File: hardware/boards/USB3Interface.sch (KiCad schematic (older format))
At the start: 7 parts, among them J2 USB3_Micro_B_Amphenol, J5 Conn_02x04_Odd_Even, U1 ECP5UM5G-381caBGA, U3 CYUSB3014, U6 128MiB

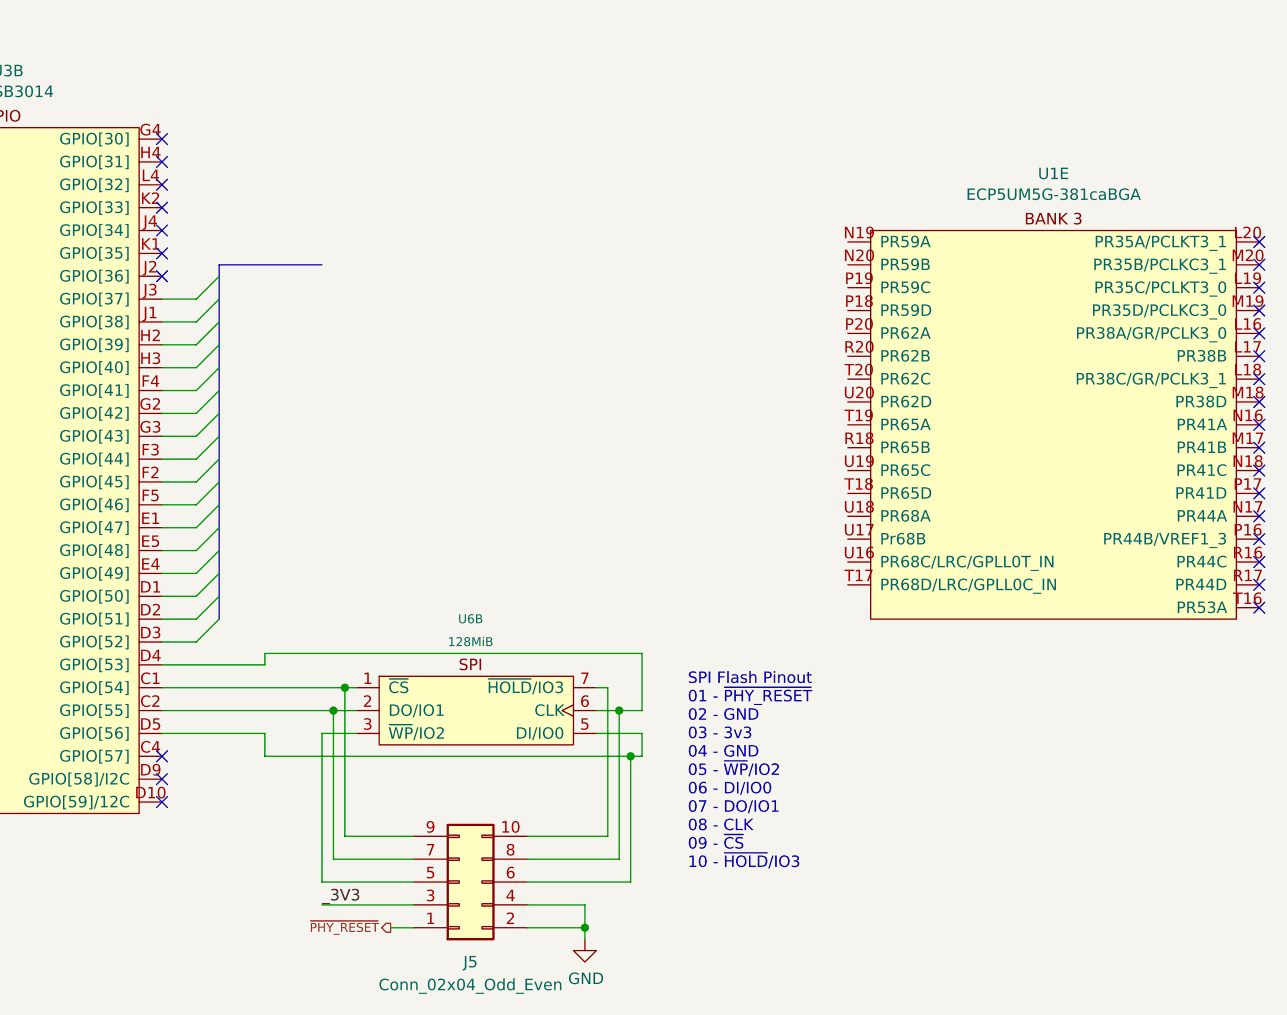
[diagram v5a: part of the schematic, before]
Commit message: Hooked up most of the GPIF II bus to the the FPGA
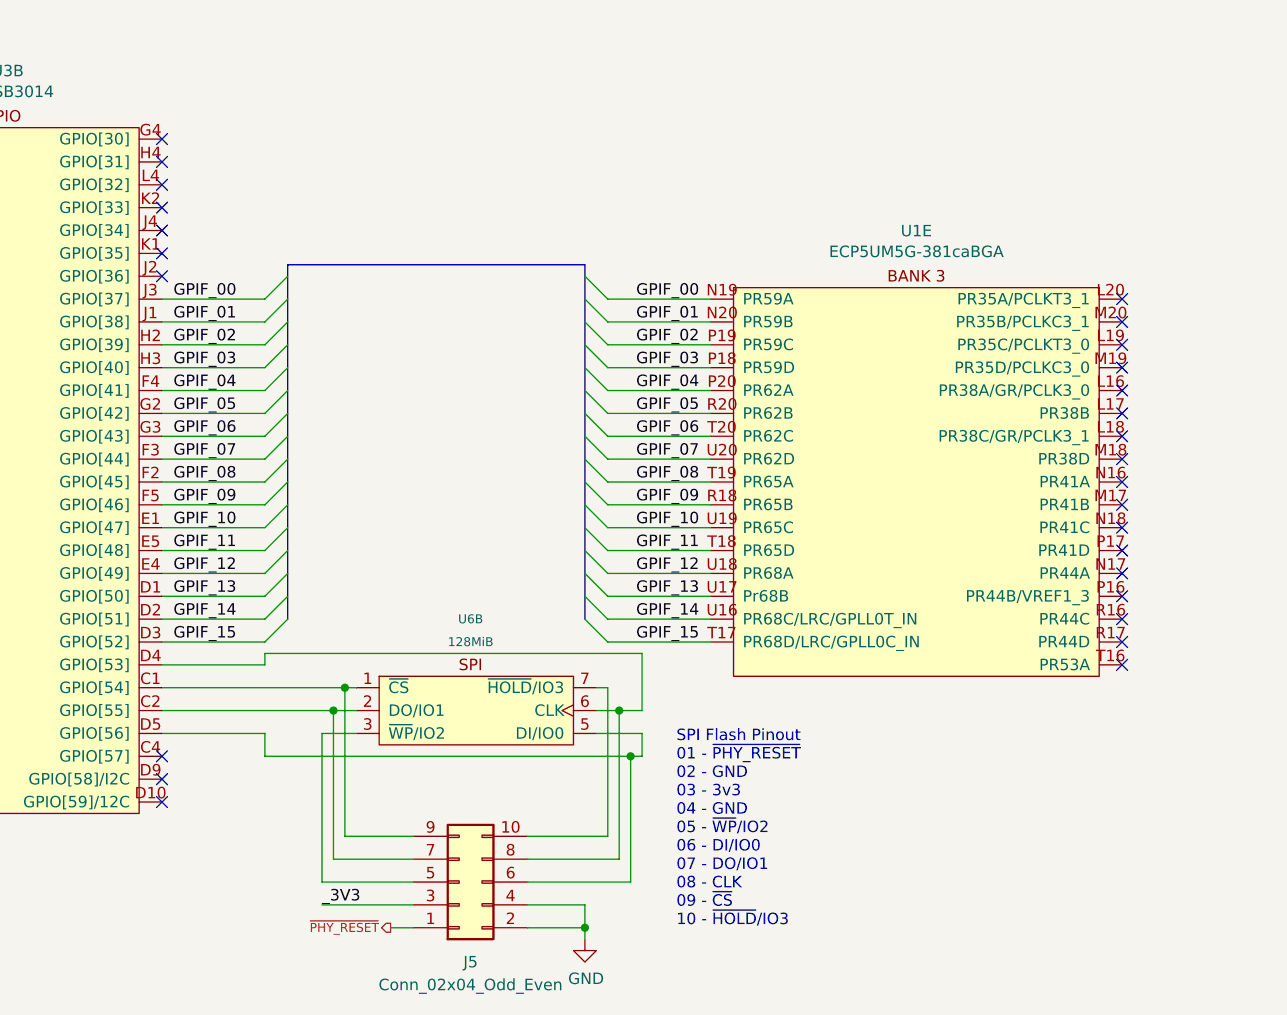
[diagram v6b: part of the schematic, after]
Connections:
- net GPIF_13: now reaches U3.D1 (GPIO[50])
- net GPIF_13: now also U1.U17 (Pr68B)
- net GPIF_14: now reaches U3.D2 (GPIO[51])
- net GPIF_14: now also U1.U16 (PR68C/LRC/GPLL0T_IN)
- net GPIF_15: now reaches U3.D3 (GPIO[52])
- net GPIF_15: now also U1.T17 (PR68D/LRC/GPLL0C_IN)
- net GPIF_10: now reaches U3.E1 (GPIO[47])
- net GPIF_10: now also U1.U19 (PR65C)
- net GPIF_12: now reaches U3.E4 (GPIO[49])
- net GPIF_12: now also U1.U18 (PR68A)
- net GPIF_11: now reaches U3.E5 (GPIO[48])
- net GPIF_11: now also U1.T18 (PR65D)
- net GPIF_08: now reaches U3.F2 (GPIO[45])
- net GPIF_08: now also U1.T19 (PR65A)
- net GPIF_07: now reaches U3.F3 (GPIO[44])
- net GPIF_07: now also U1.U20 (PR62D)
- net GPIF_04: now reaches U3.F4 (GPIO[41])
- net GPIF_04: now also U1.P20 (PR62A)
- net GPIF_09: now reaches U3.F5 (GPIO[46])
- net GPIF_09: now also U1.R18 (PR65B)
- net GPIF_05: now reaches U3.G2 (GPIO[42])
- net GPIF_05: now also U1.R20 (PR62B)
- net GPIF_06: now reaches U3.G3 (GPIO[43])
- net GPIF_06: now also U1.T20 (PR62C)
- net GPIF_02: now reaches U3.H2 (GPIO[39])
- net GPIF_02: now also U1.P19 (PR59C)
- net GPIF_03: now reaches U3.H3 (GPIO[40])
- net GPIF_03: now also U1.P18 (PR59D)
- net GPIF_01: now reaches U3.J1 (GPIO[38])
- net GPIF_01: now also U1.N20 (PR59B)
- net GPIF_00: now reaches U3.J3 (GPIO[37])
- net GPIF_00: now also U1.N19 (PR59A)
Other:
- moved on the sheet: U1E

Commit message: Moving banks around and rotated the FPGA to try and give the SERDES channels the best routing to the PCIe connector
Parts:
- removed U1: ECP5UM5G-381caBGA, lethalbit:318caBGA, symbol lethalbit:ECP5UM5G-381caBGA
- added U1: ECP5UM5G-381caBGA, lethalbit:318caBGA, symbol lethalbit:ECP5UM5G-381caBGA
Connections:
- net GPIF_00: now also U1.C18 (PR11A/URC/GPLL0T_IN)
- net GPIF_01: now also U1.D17 (PR11B/URC/GPLL0C_IN)
- net GPIF_02: now also U1.E16 (PR11C)
- net GPIF_03: now also U1.F16 (PR11D)
- net GPIF_04: now also U1.D18 (PR14A)
- net GPIF_05: now also U1.E17 (PR14B)
- net GPIF_06: now also U1.E18 (PR14C)
- net GPIF_07: now also U1.F18 (PR14D)
- net GPIF_08: now also U1.F17 (PR17A)
- net GPIF_09: now also U1.G18 (PR17B)
- net GPIF_10: now also U1.G16 (PR17C)
- net GPIF_11: now also U1.H16 (PR17D)
- net GPIF_12: now also U1.H18 (PR20A)
- net GPIF_13: now also U1.H17 (PR20B)
- net GPIF_14: now also U1.J17 (PR20C)
- net GPIF_15: now also U1.J16 (PR20D)
- no-connect marks 59 -> 58
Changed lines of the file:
@@
 NoConn ~ 5050 3950
 NoConn ~ 5050 3850
-NoConn ~ 9250 5850
 NoConn ~ 9250 5750
 NoConn ~ 9250 5650
@@
 Wire Wire Line
 	5050 5750 5500 5750
-$Comp
-L lethalbit:ECP5UM5G-381caBGA U?
-U 5 1 610C217C
-P 8350 4300
-AR Path="/5EF67D90/610C217C" Ref="U?"  Part="5"
-AR Path="/5F2CAFD2/610C217C" Ref="U1"  Part="5"
-F 0 "U1" H 8350 4648 50  0000 C CNN
-F 1 "ECP5UM5G-381caBGA" H 8350 4557 50  0000 C CNN
-F 2 "lethalbit:318caBGA" H 7000 4450 50  0001 C CNN
-F 3 "" H 7000 4450 50  0001 C CNN
-F 4 "Lattice" H 8350 4300 50  0001 C CNN "MFR"
-F 5 "LFE5UM5G-85F-8BG381I" H 8350 4300 50  0001 C CNN "MPN"
-F 6 "220-2112-ND" H 8350 4300 50  0001 C CNN "DIGIKEY_PN"
-	5    8350 4300
-	-1   0    0    -1
-$EndComp
 Text Notes 7300 7000 0    50   ~ 0
 SPI Flash Pinout\n01 - ~PHY_RESET~\n02 - GND\n03 - 3v3\n04 - GND\n05 - ~WP~/IO2\n06 - DI/IO0\n07 - DO/IO1\n08 - CLK\n09 - ~CS~\n10 - ~HOLD~/IO3\n
@@
 Text Label 5100 5650 0    50   ~ 0
 GPIF_14
-Wire Bus Line
-	6900 4100 6900 5650
-Wire Bus Line
-	5600 4100 5600 5650
 Text Label 5100 5550 0    50   ~ 0
 GPIF_13
@@
 Text Label 7400 4250 2    50   ~ 0
 GPIF_00
+$Comp
+L lethalbit:ECP5UM5G-381caBGA U?
+U 4 1 5F8956D3
+P 8350 4300
+AR Path="/5EF6A128/5F8956D3" Ref="U?"  Part="4"
+AR Path="/5F2CAFD2/5F8956D3" Ref="U1"  Part="4"
+F 0 "U1" H 8350 4648 50  0000 C CNN
+F 1 "ECP5UM5G-381caBGA" H 8350 4557 50  0000 C CNN
+F 2 "lethalbit:318caBGA" H 7000 4450 50  0001 C CNN
+F 3 "" H 7000 4450 50  0001 C CNN
+F 4 "Lattice" H 8350 4300 50  0001 C CNN "MFR"
+F 5 "LFE5UM5G-85F-8BG381I" H 8350 4300 50  0001 C CNN "MPN"
+F 6 "220-2112-ND" H 8350 4300 50  0001 C CNN "DIGIKEY_PN"
+	4    8350 4300
+	1    0    0    -1
+$EndComp
+Wire Bus Line
+	6900 4100 6900 5650
+Wire Bus Line
+	5600 4100 5600 5650
 $EndSCHEMATC

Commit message: Moved some things around swapping the DDR from banks 7 and 8 to banks 2 and 3, and moved the GPIFF 2 stuff to bank 7 to stop them from crossing over
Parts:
- removed U1: ECP5UM5G-381caBGA, lethalbit:318caBGA, symbol lethalbit:ECP5UM5G-381caBGA
- added U1: ECP5UM5G-381caBGA, lethalbit:318caBGA, symbol lethalbit:ECP5UM5G-381caBGA
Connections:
- net GPIF_00: now also U1.G3 (PL32A/PCLKT7_1)
- net GPIF_01: now also U1.F3 (PL32B/PCLKC7_1)
- net GPIF_02: now also U1.F2 (PL32C/PCLKT7_0)
- net GPIF_03: now also U1.E2 (PL32D/PCLKC7_0)
- net GPIF_04: now also U1.H4 (PL29A/GR/PCLK7_1)
- net GPIF_05: now also U1.G5 (PL29B)
- net GPIF_06: now also U1.H5 (PL29C/GR/PCLK7_0)
- net GPIF_07: now also U1.H3 (PL29D)
- net GPIF_08: now also U1.C1 (PL26A)
- net GPIF_09: now also U1.D1 (PL26B)
- net GPIF_10: now also U1.D2 (PL26C)
- net GPIF_11: now also U1.E1 (PL26D)
- net GPIF_12: now also U1.A2 (PL23A)
- net GPIF_13: now also U1.B1 (PL23B)
- net GPIF_14: now also U1.B2 (PL23C/VREF1_7)
- net GPIF_15: now also U1.C2 (PL23D)
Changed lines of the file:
@@
 $Comp
 L lethalbit:ECP5UM5G-381caBGA U?
-U 4 1 5F8956D3
+U 7 1 5FC843C8
 P 8350 4300
-AR Path="/5EF6A128/5F8956D3" Ref="U?"  Part="4"
-AR Path="/5F2CAFD2/5F8956D3" Ref="U1"  Part="4"
+AR Path="/5EDF3898/5FC843C8" Ref="U?"  Part="7"
+AR Path="/5FC843C8" Ref="U?"  Part="7"
+AR Path="/5F2CAFD2/5FC843C8" Ref="U1"  Part="7"
 F 0 "U1" H 8350 4648 50  0000 C CNN
 F 1 "ECP5UM5G-381caBGA" H 8350 4557 50  0000 C CNN
@@
 F 5 "LFE5UM5G-85F-8BG381I" H 8350 4300 50  0001 C CNN "MPN"
 F 6 "220-2112-ND" H 8350 4300 50  0001 C CNN "DIGIKEY_PN"
-	4    8350 4300
+	7    8350 4300
 	1    0    0    -1
 $EndComp
